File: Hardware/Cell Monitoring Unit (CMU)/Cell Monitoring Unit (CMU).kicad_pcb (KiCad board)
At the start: 4 copper layers, 144.7 x 95.9 mm, 186 parts, among them J1 705550056, J10 NTC-6, J11 NTC-7, J12 NTC-8, J2 JUMPER, J3 HIGH SIDE, J4 LOW SIDE, J5 NTC-1, J6 NTC-2, J7 NTC-3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

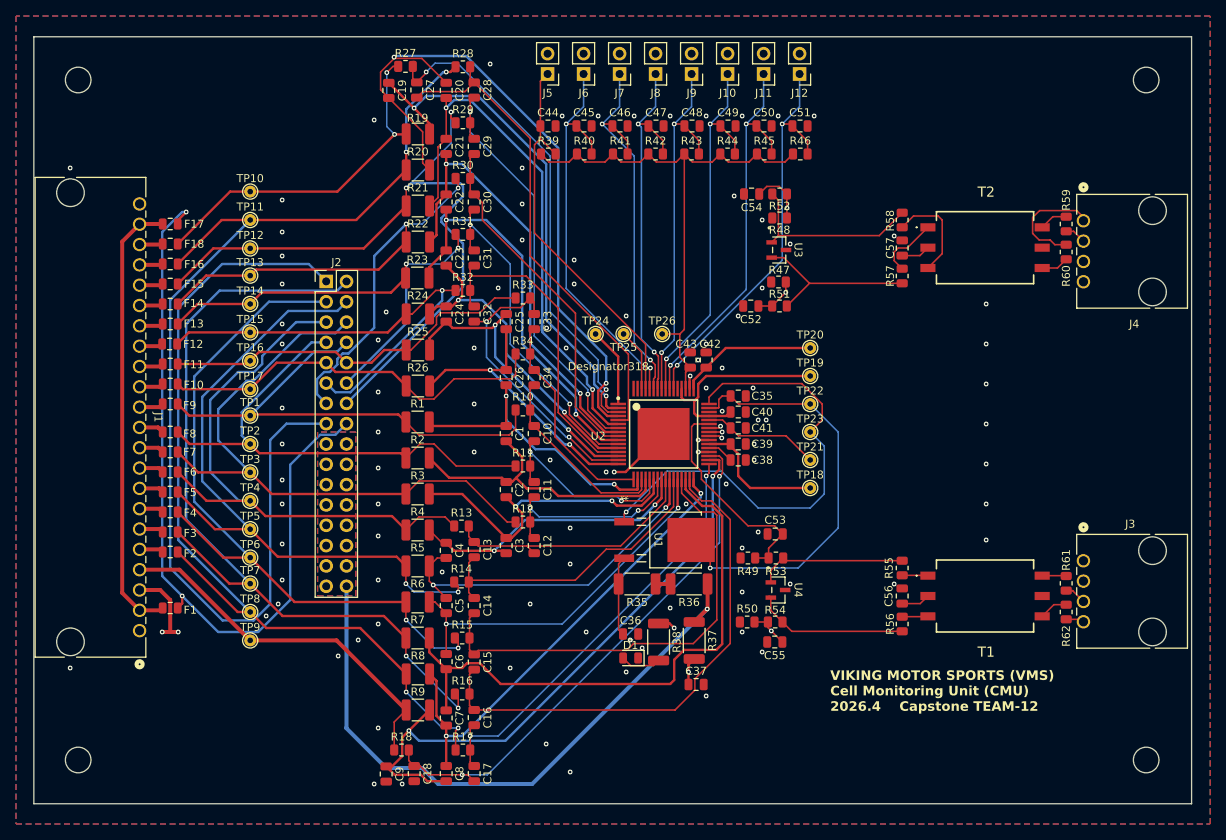
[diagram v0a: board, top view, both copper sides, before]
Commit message: Rounded corners, better board silk, stitching vias
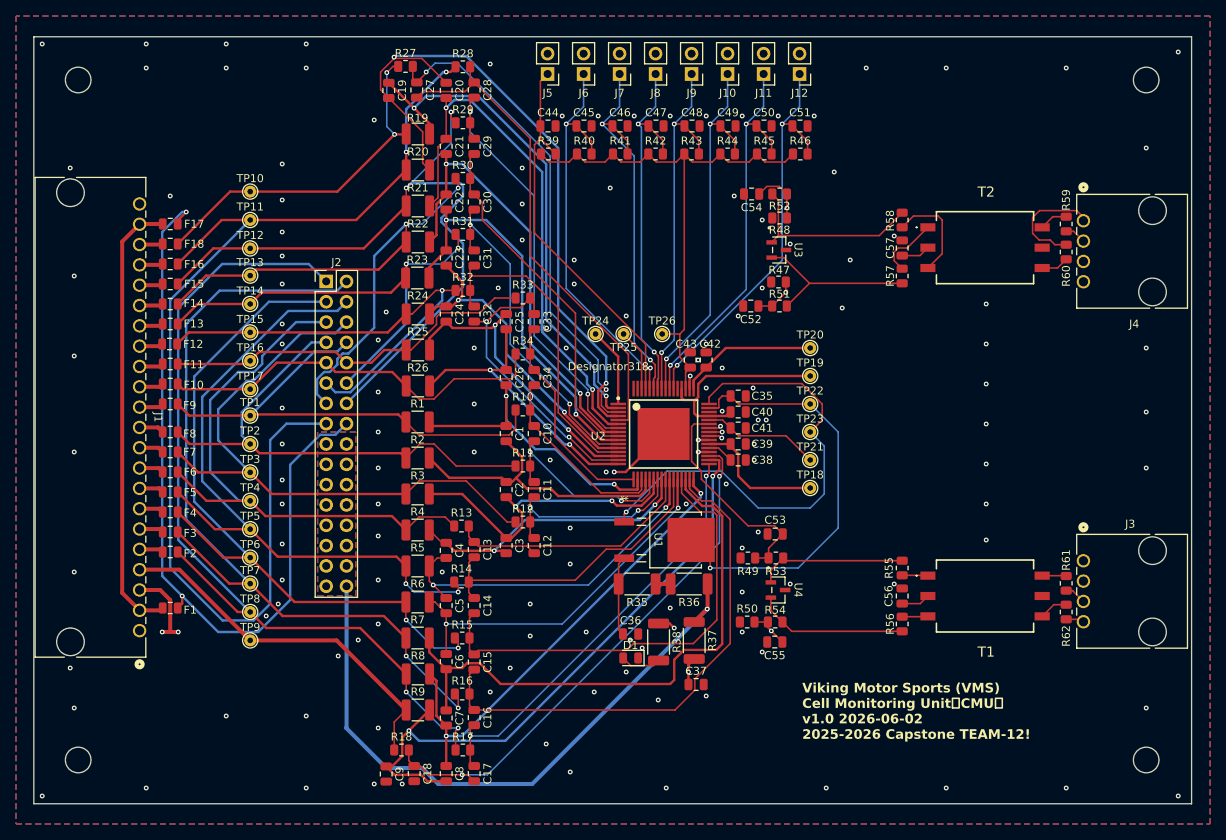
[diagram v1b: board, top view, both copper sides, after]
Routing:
- net CELL0: vias 105 -> 146
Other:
- board text added: "${COMPANY} ${TITLE} v${REVISION} ${ISSUE_DATE} 2025-2026 Capstone TEAM-12!"
- board text removed: "VIKING MOTOR SPORTS (VMS) Cell Monitoring Unit (CMU) 2026.4 Capstone TEAM-12"
